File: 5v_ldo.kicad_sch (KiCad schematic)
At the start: 3 parts, among them U1401 MG78L05T3

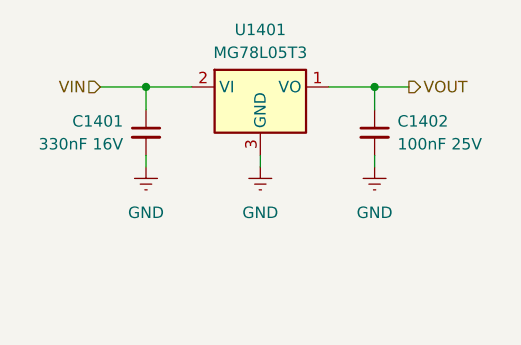
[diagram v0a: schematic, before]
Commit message: adding test pads + minor schematic edits
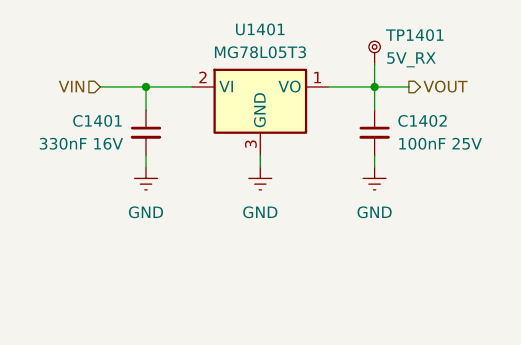
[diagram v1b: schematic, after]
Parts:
- added TP1401: 5V_RX, BR_Connectors:TEST-TH_BD2.54-P1.4_RED, symbol BR_Connectors:TP_Ring_PTH
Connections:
- net VOUT: now also TP1401.1
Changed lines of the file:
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@@
+	(wire
+		(pts
+			(xy 116.84 57.15) (xy 116.84 59.69)
+		)
+		(stroke
+			(width 0)
+			(type default)
+		)
+	)
 	(wire
 		(pts
@@
 					(unit 1)
 				)
+			)
+		)
+	)
+	(symbol
+		(lib_id "BR_Connectors:TP_Ring_PTH")
+		(at 116.84 57.15 0)
+		(unit 1)
+		(exclude_from_sim no)
+		(in_bom yes)
+		(on_board yes)
+		(dnp no)
+		(fields_autoplaced yes)
+		(property "Reference" "TP1401"
+			(at 118.11 53.9749 0)
+			(effects
+				(font
+					(size 1.27 1.27)
+				)
+				(justify left)
+			)
+		)
+		(property "Value" "5V_RX"
+			(at 118.11 56.5149 0)
+			(effects
+				(font
+					(size 1.27 1.27)
+				)
+				(justify left)
+			)
+		)
+		(property "Footprint" "BR_Connectors:TEST-TH_BD2.54-P1.4_RED"
+			(at 116.84 -19.05 0)
+			(effects
+				(font
+					(size 1.27 1.27)
+				)
+				(justify left)
+				(hide yes)
+			)
+		)
+		(property "Datasheet" "https://wmsc.lcsc.com/wmsc/upload/file/pdf/v2/lcsc/2307040929_ronghe-RH-5000_C5277086.pdf"
+			(at 116.84 -16.51 0)
+			(effects
+				(font
+					(size 1.27 1.27)
+				)
+				(justify left)
+				(hide yes)
+			)
+		)
+		(property "Description" "Ring Test Point for Probe(s) PTH"
+			(at 116.84 -13.97 0)
+			(effects
+				(font
+					(size 1.27 1.27)
+				)
+				(justify left)
+				(hide yes)
+			)
+		)
+		(property "Manufacturer" "ronghe"
+			(at 116.84 -11.43 0)
+			(effects
+				(font
+					(size 1.27 1.27)
+				)
+				(justify left)
+				(hide yes)
+			)
+		)
+		(property "Manufacturer Part Num" "RH-5000"
+			(at 116.84 -8.89 0)
+			(effects
+				(font
+					(size 1.27 1.27)
+				)
+				(justify left)
+				(hide yes)
+			)
+		)
+		(property "BRE Number" "BRE-000074"
+			(at 116.84 -6.35 0)
+			(effects
+				(font
+					(size 1.27 1.27)
+				)
+				(justify left)
+				(hide yes)
+			)
+		)
+		(property "Supplier 1" "DigiKey"
+			(at 116.84 -3.81 0)
+			(effects
+				(font
+					(size 1.27 1.27)
+				)
+				(justify left)
+				(hide yes)
+			)
+		)
+		(property "Supplier Part Num 1" "~"
+			(at 116.84 -1.27 0)
+			(effects
+				(font
+					(size 1.27 1.27)
+				)
+				(justify left)
+				(hide yes)
+			)
+		)
+		(property "Supplier 2" "Mouser"
+			(at 116.84 1.27 0)
+			(effects
+				(font
+					(size 1.27 1.27)
+				)
+				(justify left)
+				(hide yes)
+			)
+		)
+		(property "Supplier Part Num 2" "~"
+			(at 116.84 3.81 0)
+			(effects
+				(font
+					(size 1.27 1.27)
+				)
+				(justify left)
+				(hide yes)
+			)
+		)
+		(property "Supplier 3" "JLCPCB"
+			(at 116.84 6.35 0)
+			(effects
+				(font
+					(size 1.27 1.27)
+				)
+				(justify left)
+				(hide yes)
+			)
+		)
+		(property "Supplier Part Num 3" "C5277086"
+			(at 116.84 8.89 0)
+			(effects
+				(font
+					(size 1.27 1.27)
+				)
+				(justify left)
+				(hide yes)
+			)
+		)
+		(property "Label" "LABEL"
+			(at 116.84 11.43 0)
+			(effects
+				(font
+					(size 1.27 1.27)
+				)
+				(justify left)
+				(hide yes)
+			)
+		)
+		(property "JLCPCB Part Num" "C5277086"
+			(at 116.84 13.97 0)
+			(effects
+				(font
+					(size 1.27 1.27)
+				)
+				(justify left)
+				(hide yes)
+			)
+		)
+		(pin "1"
+		)
+		(instances
+			(project ""
+				(path "/2a5ce3ef-537a-4122-a1be-ef76186bc0d7/774f2c6c-c15c-4713-acf0-4edb2ec6be20/d89bd557-813e-4016-ac7f-80185426a1bc"
+					(reference "TP1401")
+					(unit 1)
+				)

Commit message: last checks + board characteristics tables
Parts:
- added TP1402: GND, BR_Connectors:TEST-TH_BD2.54-P1.4_RED, symbol BR_Connectors:TP_Ring_PTH
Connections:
- net GND: now also TP1402.1
